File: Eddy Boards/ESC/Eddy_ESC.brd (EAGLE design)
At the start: 101.6 x 102.9 mm, 24 parts

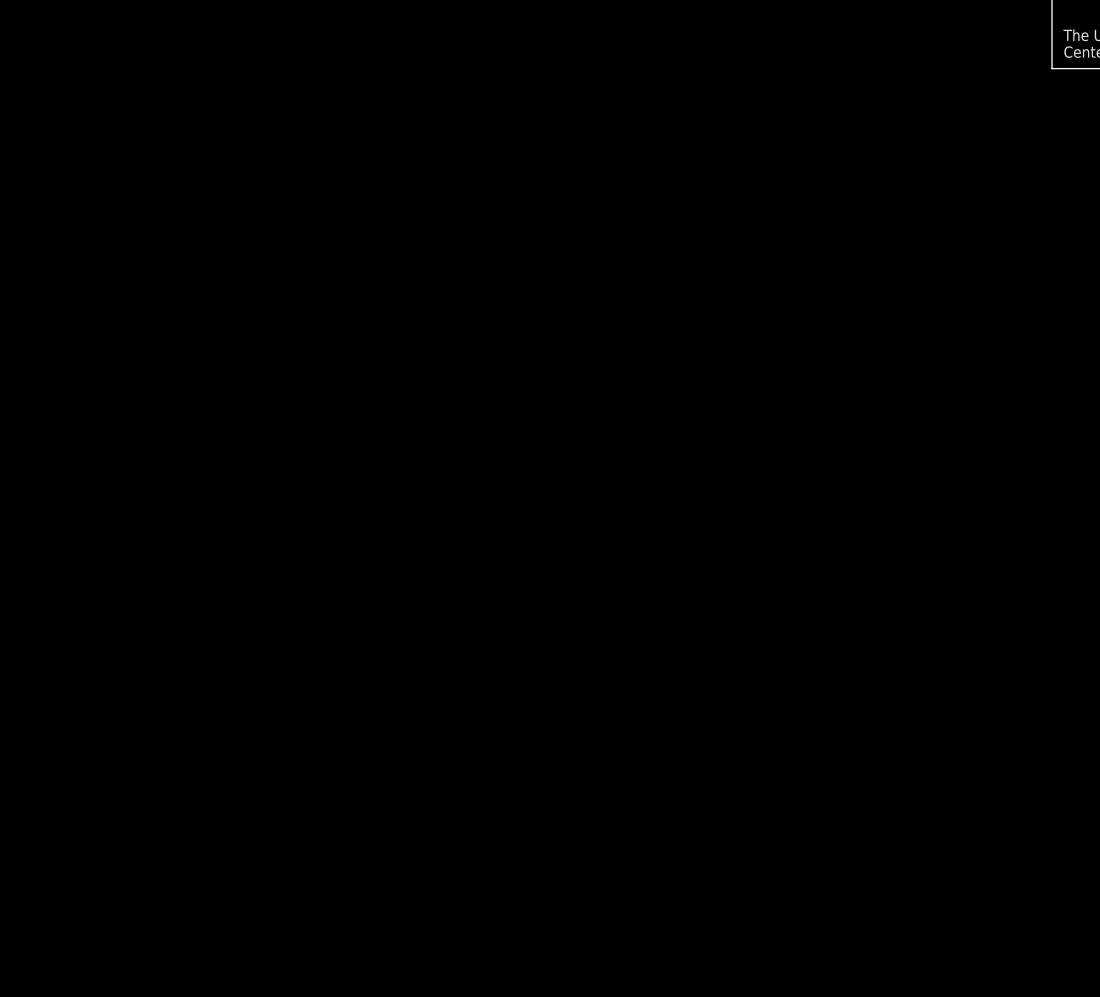
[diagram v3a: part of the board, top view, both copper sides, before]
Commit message: started sheet 2 of schematic, need explanation of esc's the alternating setup is confusing me. Need labels on sheet 1
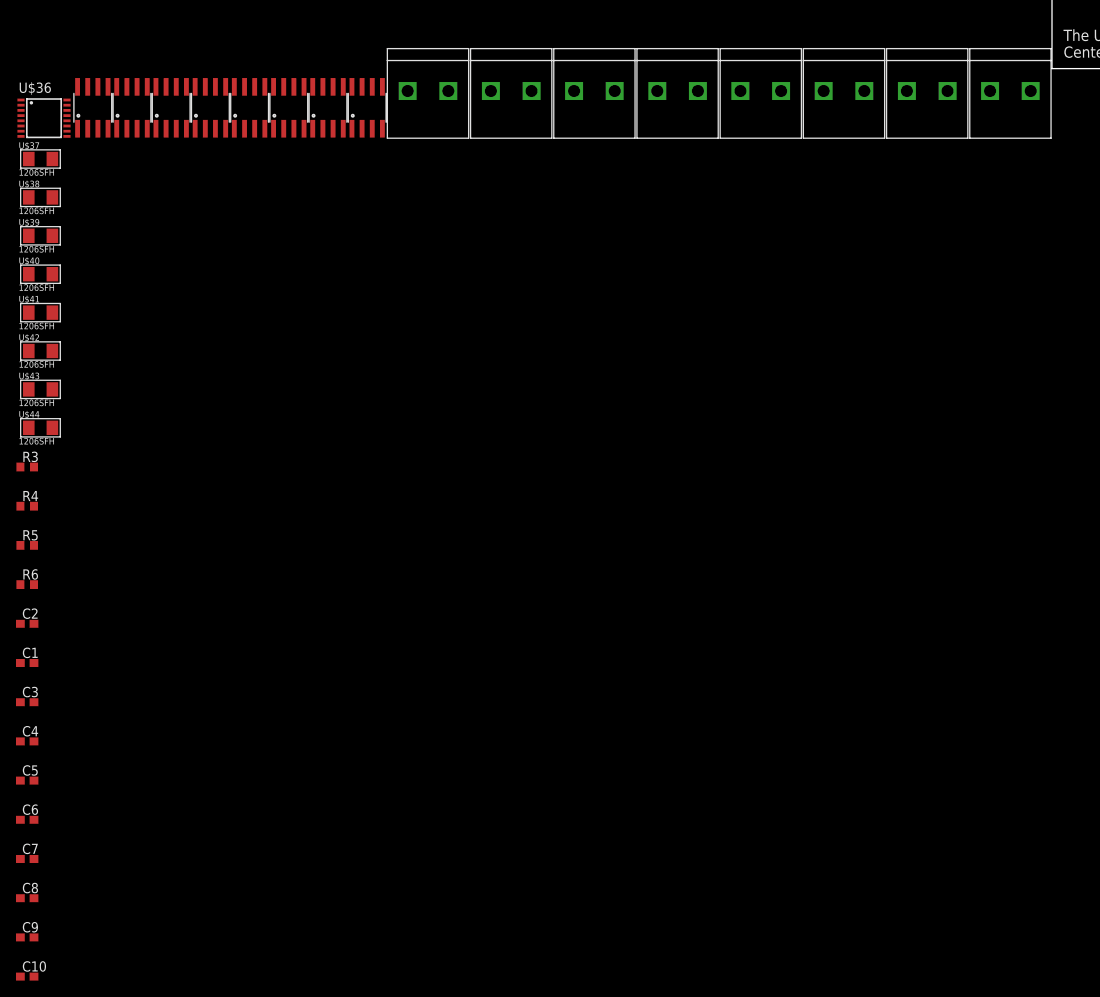
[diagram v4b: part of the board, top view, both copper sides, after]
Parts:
- added C1, C2, C3, C4, C5, C6, C7, C8, C9: 0.1uF, rcl:C0603
- added C10: 1uF, rcl:C0603
- added R3, R4, R5, R6: 900, resistor:R0603
- added U$20, U$21, U$22, U$23, U$24, U$25, U$26, U$27: 1711725, Screw_Terminals:1711725
- added U$28, U$29, U$30, U$31, U$32, U$33, U$34, U$35: ACS722, ACS722:SOIC-8
- added U$36: ADC128D818, ADC128D818:TSSOP-16
- added U$37, U$38, U$39, U$40, U$41, U$42, U$43, U$44: 1206SFH, 1206SFH:1206SFH
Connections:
- new net N$37: U$34.VIOUT, U$36.IN4
- new net N$38: U$29.VIOUT, U$36.IN3
- new net N$40: U$33.IP-1, U$33.IP-2, U$38.P$2
- new net N$41: U$34.IP-1, U$34.IP-2, U$39.P$2
- new net N$42: U$31.VIOUT, U$36.IN7
- new net N$43: U$35.VIOUT, U$36.IN6
- new net N$45: U$30.VIOUT, U$36.IN5
- new net N$46: U$32.IP-1, U$32.IP-2, U$37.P$2
- new net N$47: U$35.IP-1, U$35.IP-2, U$40.P$2
- new net N$48: U$33.VIOUT, U$36.IN2
- new net N$49: U$28.VIOUT, U$36.IN1
- new net N$50: U$32.VIOUT, U$36.IN0
- new net N$51: U$24.RED, U$37.P$1
- new net N$52: U$25.RED, U$38.P$1
- new net N$53: U$26.RED, U$39.P$1
- new net N$54: U$27.RED, U$40.P$1
- new net N$55: U$20.RED, U$41.P$1
- new net N$56: U$21.RED, U$42.P$1
- new net N$57: U$22.RED, U$43.P$1
- new net N$58: U$23.RED, U$44.P$1
- net +3V3: now also C1.2, C10.1, C2.2, C3.2, C4.2, C5.2, C6.2, C7.2, C8.2, C9.1, U$36.V+, U$36.VREF
- net GND: now also C1.1, C10.2, C2.1, C3.1, C4.1, C5.1, C6.1, C7.1, C8.1, C9.2

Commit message: temporary
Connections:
- new net N$59: R5.1, R6.2, U$36.A0
- new net N$60: R3.2, R4.2, U$36.A1
- new net N$61: U$36.SDA
- new net N$62: U$36.SCL
- net +3V3: now also R4.1, R6.1
- net GND: now also R3.1, R5.2, U$36.GND
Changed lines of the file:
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@@
 <contactref element="C9" pad="2"/>
 <contactref element="C10" pad="2"/>
+<contactref element="U$36" pad="GND"/>
+<contactref element="R5" pad="2"/>
+<contactref element="R3" pad="1"/>
 <wire x1="-127.25" y1="-100.8" x2="-127.25" y2="-105.7" width="0" layer="19" extent="1-1"/>
 <wire x1="-128.95" y1="-95.9" x2="-127.25" y2="-100.8" width="0" layer="19" extent="1-1"/>
@@
 <wire x1="-128.95" y1="-66.5" x2="-128.95" y2="-71.4" width="0" layer="19" extent="1-1"/>
 <wire x1="-128.95" y1="-61.6" x2="-128.95" y2="-66.5" width="0" layer="19" extent="1-1"/>
-<wire x1="24.1455" y1="3.375" x2="-128.95" y2="-61.6" width="0" layer="19" extent="1-16"/>
+<wire x1="-127.25" y1="-51.8" x2="-128.95" y2="-61.6" width="0" layer="19" extent="1-1"/>
+<wire x1="-128.95" y1="-42" x2="-127.25" y2="-51.8" width="0" layer="19" extent="1-1"/>
+<wire x1="-128.875" y1="1.925" x2="-128.95" y2="-42" width="0" layer="19" extent="1-1"/>
+<wire x1="18.3" y1="16.95" x2="-128.875" y2="1.925" width="0" layer="19" extent="1-1"/>
+<wire x1="26.67" y1="7.62" x2="18.3" y2="16.95" width="0" layer="19" extent="1-1"/>
+<wire x1="26.6855" y1="3.375" x2="26.67" y2="7.62" width="0" layer="19" extent="16-16"/>
 <wire x1="36.957" y1="7.62" x2="36.8455" y2="3.375" width="0" layer="19" extent="16-16"/>
-<wire x1="26.67" y1="7.62" x2="26.6855" y2="3.375" width="0" layer="19" extent="16-16"/>
-<wire x1="18.3" y1="16.95" x2="26.67" y2="7.62" width="0" layer="19" extent="1-1"/>
 <wire x1="42.916509375" y1="93.161740625" x2="18.3" y2="16.95" width="0" layer="19" extent="1-1"/>
 <wire x1="47.116409375" y1="93.132421875" x2="42.916509375" y2="93.161740625" width="0" layer="19" extent="1-1"/>
@@
 <contactref element="U$36" pad="VREF"/>
 <contactref element="U$36" pad="V+"/>
+<contactref element="R4" pad="1"/>
+<contactref element="R6" pad="1"/>
 <wire x1="-128.95" y1="-100.8" x2="-128.95" y2="-105.7" width="0" layer="19" extent="1-1"/>
 <wire x1="-127.25" y1="-95.9" x2="-128.95" y2="-100.8" width="0" layer="19" extent="1-1"/>
@@
 <wire x1="-127.25" y1="-66.5" x2="-127.25" y2="-71.4" width="0" layer="19" extent="1-1"/>
 <wire x1="-127.25" y1="-61.6" x2="-127.25" y2="-66.5" width="0" layer="19" extent="1-1"/>
-<wire x1="-128.875" y1="1.275" x2="-127.25" y2="-61.6" width="0" layer="19" extent="1-1"/>
+<wire x1="-128.95" y1="-56.7" x2="-127.25" y2="-61.6" width="0" layer="19" extent="1-1"/>
+<wire x1="-128.95" y1="-46.9" x2="-128.95" y2="-56.7" width="0" layer="19" extent="1-1"/>
+<wire x1="-128.875" y1="1.275" x2="-128.95" y2="-46.9" width="0" layer="19" extent="1-1"/>
 <wire x1="-128.875" y1="3.875" x2="-128.875" y2="1.275" width="0" layer="19" extent="1-1"/>
 <wire x1="16.5255" y1="3.375" x2="-128.875" y2="3.875" width="0" layer="19" extent="1-1"/>
@@
 <wire x1="-33.86" y1="5" x2="-127.9" y2="-37.1" width="0" layer="19" extent="1-1"/>
 </signal>
+<signal name="N$59">
+<contactref element="U$36" pad="A0"/>
+<contactref element="R5" pad="1"/>
+<contactref element="R6" pad="2"/>
+<wire x1="-128.95" y1="-51.8" x2="-127.25" y2="-56.7" width="0" layer="19" extent="1-1"/>
+<wire x1="-128.875" y1="-0.025" x2="-128.95" y2="-51.8" width="0" layer="19" extent="1-1"/>
+</signal>
+<signal name="N$60">
+<contactref element="U$36" pad="A1"/>
+<contactref element="R4" pad="2"/>
+<contactref element="R3" pad="2"/>
+<wire x1="-127.25" y1="-42" x2="-127.25" y2="-46.9" width="0" layer="19" extent="1-1"/>
+<wire x1="-128.875" y1="-0.675" x2="-127.25" y2="-42" width="0" layer="19" extent="1-1"/>
+</signal>
+<signal name="N$61">
+<contactref element="U$36" pad="SDA"/>
+</signal>
+<signal name="N$62">
+<contactref element="U$36" pad="SCL"/>
+</signal>
 </signals>
